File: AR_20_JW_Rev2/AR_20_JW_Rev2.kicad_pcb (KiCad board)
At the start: 2 copper layers, 85.1 x 58.4 mm, 14 parts, among them J1 Green LED, U1 ATmega328P-PU, U2 ICSP, U3 MCP2515_CAN, U4 INPUT, U5 SWITCH, Y1 16 MHz Crystal

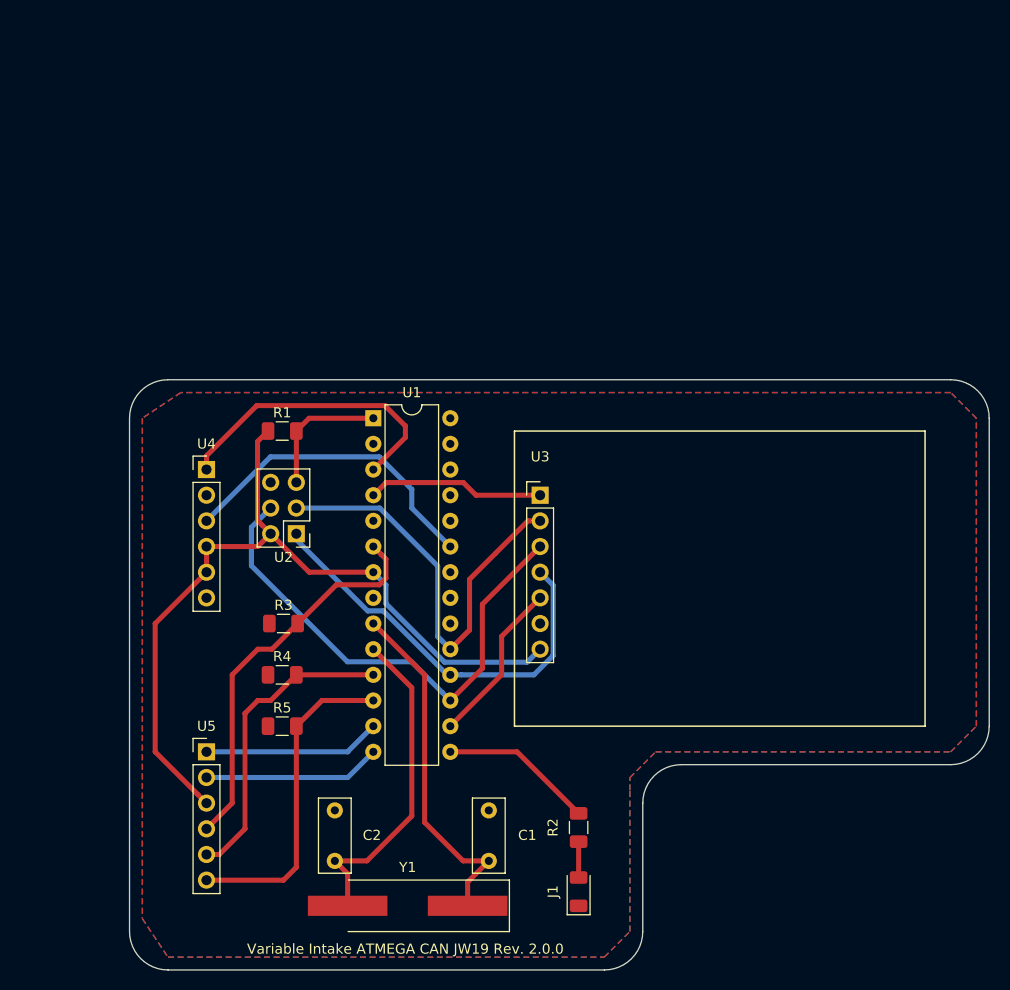
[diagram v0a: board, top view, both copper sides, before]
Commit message: Generated CAD model of board
Exported .step file of board and generated model to use in Solidworks
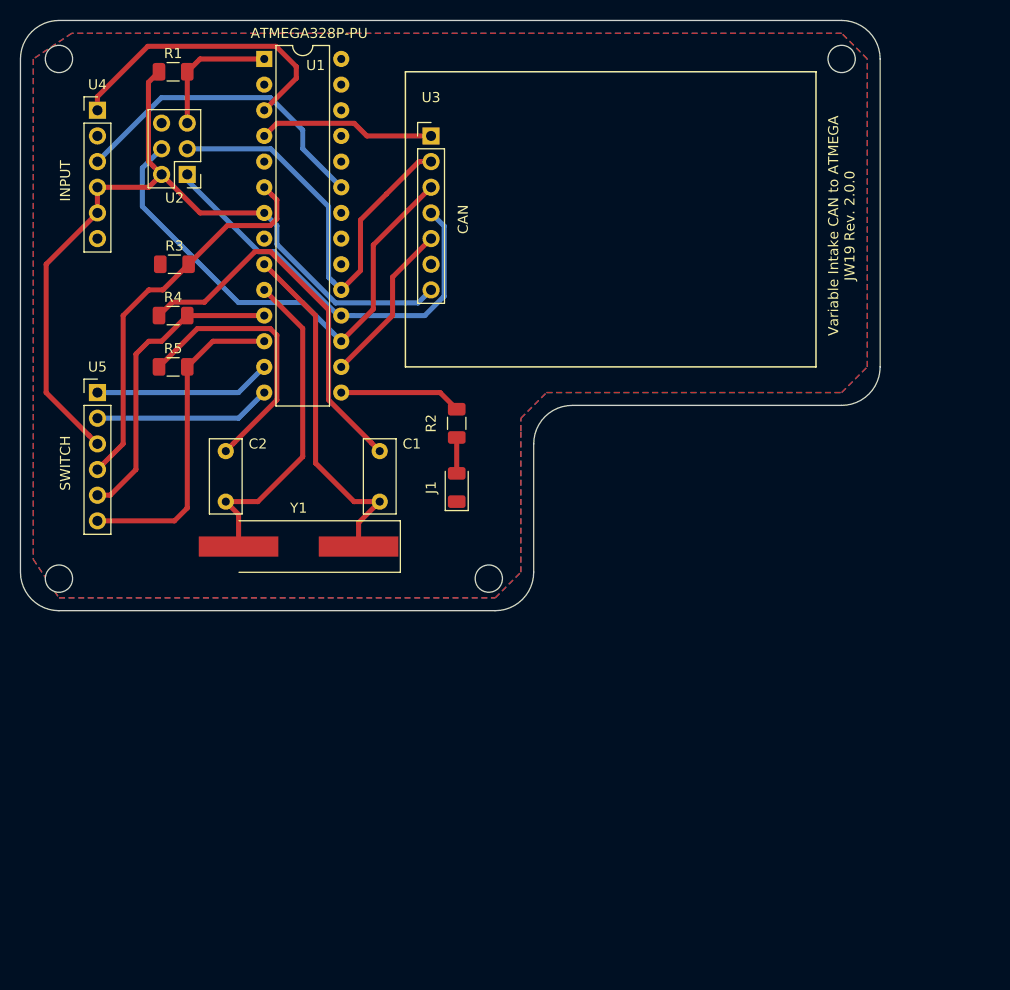
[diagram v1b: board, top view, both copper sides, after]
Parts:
- added ?: MountingHole_2.7mm_M2.5, MountingHole:MountingHole_2.7mm_M2.5, F.Cu at (149.9, 126.4)
- added ?: MountingHole_2.7mm_M2.5, MountingHole:MountingHole_2.7mm_M2.5, F.Cu at (107.3, 74.9)
- added ?: MountingHole_2.7mm_M2.5, MountingHole:MountingHole_2.7mm_M2.5, F.Cu at (107.3, 126.4)
- added ?: MountingHole_2.7mm_M2.5, MountingHole:MountingHole_2.7mm_M2.5, F.Cu at (184.8, 74.9)
- moved J1 41.8 mm to (146.7, 117.3)
- moved R2 41.8 mm to (146.7, 111.0)
- moved C1 37.2 mm to (139.1, 113.7)
- moved C2 37.2 mm to (123.8, 113.7)
- moved R1 37.2 mm to (118.6, 76.2)
- moved R3 37.2 mm to (118.7, 95.2)
- moved R5 37.2 mm to (118.6, 105.4)
- moved U2 37.2 mm to (120.0, 86.4)
- moved U3 37.2 mm to (144.1, 82.5)
- moved Y1 37.2 mm to (131.0, 123.2)
- moved R4 37.2 mm to (118.6, 100.3)
- moved U1 37.2 mm to (127.6, 74.9)
- moved U4 37.2 mm to (111.1, 80.0)
- moved U5 37.2 mm to (111.1, 108.0)
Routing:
- net GND: track 0.00 -> 65.0 mm
- net Net-(R2-Pad2): track 15.2 -> 12.1 mm
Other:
- board text added: "ATMEGA328P-PU"
- board text added: "CAN"
- board text added: "INPUT"
- board text added: "SWITCH"
- board text added: "Variable Intake CAN to ATMEGA JW19 Rev. 2.0.0"
- board text removed: "Variable Intake ATMEGA CAN JW19 Rev. 2.0.0"
